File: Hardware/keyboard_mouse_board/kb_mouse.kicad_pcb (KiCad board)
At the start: 2 copper layers, 80.8 x 60.1 mm, 27 parts, among them J1 Conn_01x40, J3 AVR-ISP-6, U1 74HC74, U2 ATmega328P-P, U3 DS1307+, U4 74HC245, Y1 32,768kHz

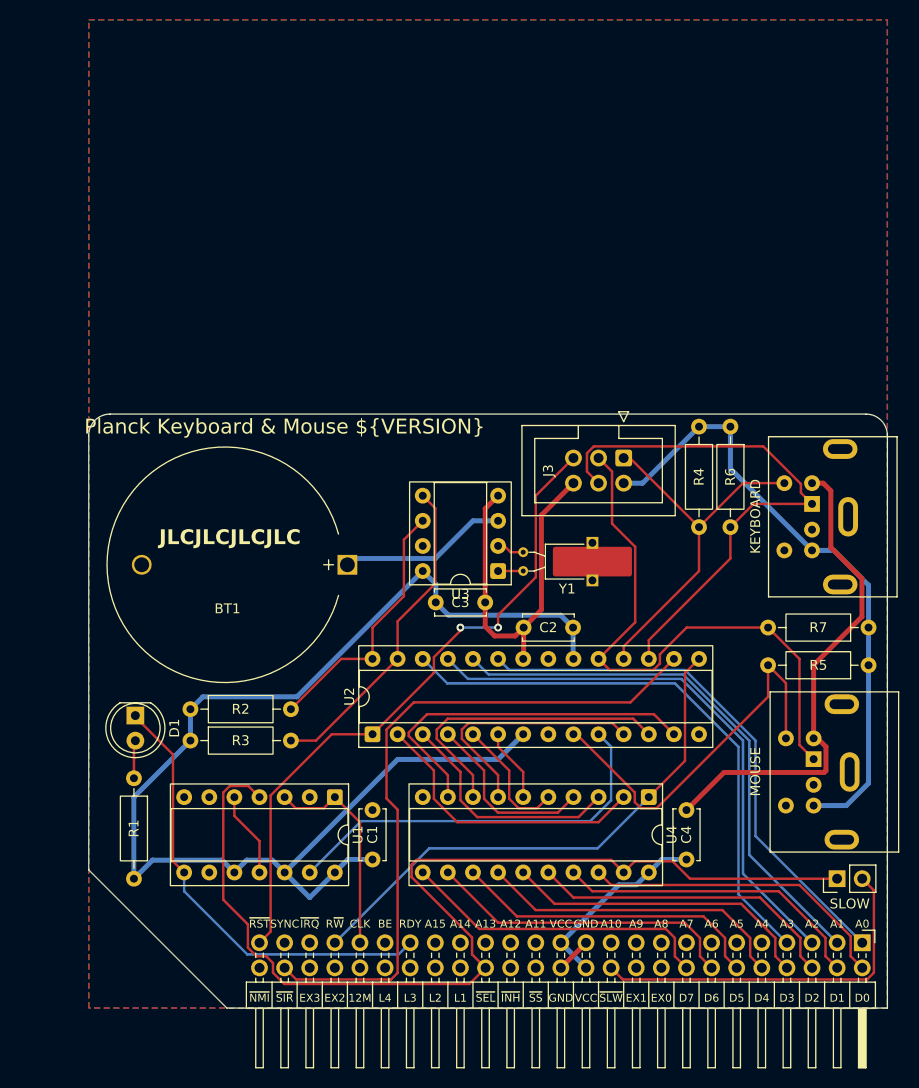
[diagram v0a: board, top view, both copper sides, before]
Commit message: RDY latch fix
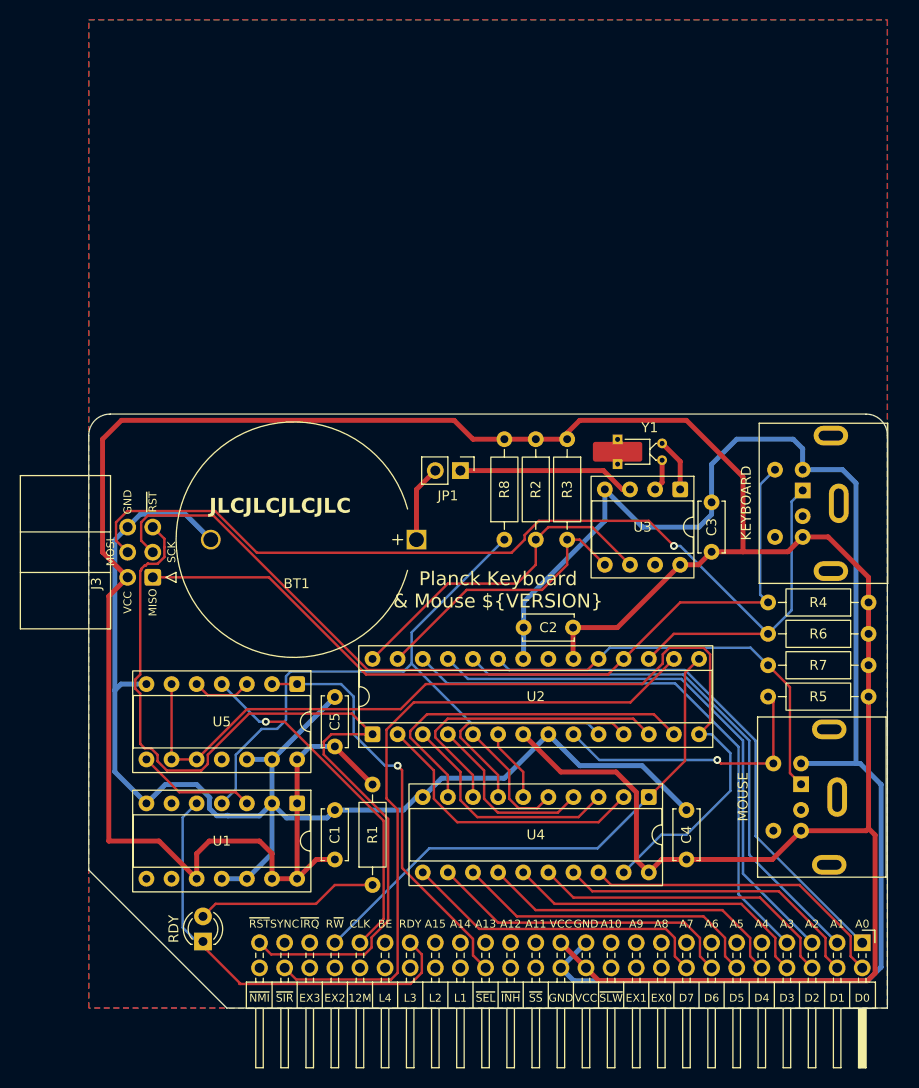
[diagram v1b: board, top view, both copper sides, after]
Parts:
- removed D1: LED, LED_THT:LED_D5.0mm
- removed SLOW: Conn_01x02, Connector_PinHeader_2.54mm:PinHeader_1x02_P2.54mm_Vertical
- added C5: 100n, Capacitor_THT:C_Disc_D5.0mm_W2.5mm_P5.00mm, F.Cu at (130.2, 111.1)
- added JP1: CLK_RESET, Connector_PinHeader_2.54mm:PinHeader_1x02_P2.54mm_Vertical, F.Cu at (142.9, 83.2)
- added R8: 10k, Resistor_THT:R_Axial_DIN0207_L6.3mm_D2.5mm_P10.16mm_Horizontal, F.Cu at (147.3, 90.2)
- added RDY: LED, LED_THT:LED_D3.0mm, F.Cu at (116.8, 130.8)
- added U5: 74HC00, Package_DIP:DIP-14_W7.62mm_Socket, F.Cu at (126.4, 104.8)
- J3: footprint Connector_IDC:IDC-Header_2x03_P2.54mm_Vertical -> Connector_IDC:IDC-Header_2x03_P2.54mm_Horizontal
- Y1: footprint Crystal:Crystal_C38-LF_D3.0mm_L8.0mm_Horizontal_1EP_style2 -> Crystal:Crystal_DS15_D1.5mm_L5.0mm_Horizontal_1EP_style2
- moved J3 49.1 mm to (111.8, 94.0), turned to 180 degrees
- moved R3 48.8 mm to (153.7, 80.0), turned to -90 degrees
- moved R2 44.3 mm to (150.5, 80.0), turned to -90 degrees
- moved C3 28.4 mm to (168.3, 91.4), turned to 90 degrees
- moved R1 26.4 mm to (134.0, 125.1), turned to 90 degrees
- moved R6 25.2 mm to (184.2, 99.7), turned to 180 degrees
- moved R4 24.7 mm to (184.2, 96.5), turned to 180 degrees
- moved U3 20.2 mm to (165.1, 85.1), turned to -90 degrees
- moved Y1 19.1 mm to (163.3, 80.4), turned to -90 degrees
- moved BT1 7.43 mm to (138.4, 90.2)
- moved U1 3.87 mm to (126.4, 116.8)
- moved C1 3.81 mm to (130.2, 122.5)
- moved LOGO 3.81 mm to (125.1, 81.2)
- moved OPENHARDWARE 3.81 mm to (121.6, 92.3)
- moved R7 3.81 mm to (184.2, 102.9)
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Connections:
- U1 pad 1: CLK -> +5V
- U1 pad 11: Net-(U1A-Q) -> GND
- U1 pad 12: +5V -> GND
- U1 pad 13: RDY_STROBE -> +5V
- U1 pad 3: CLK -> CS
- U1 pad 4: ~{SLOT_SEL} -> RDY_STROBE
- U1 pad 5: Net-(U1A-Q) -> RDY
- U1 pad 8: RDY -> unconnected-(U1B-~{Q}-Pad8)
- U2 pad 14: CSEL -> ~{CS}
- U3 pad 3: Net-(BT1-+) -> Net-(JP1-A)
- U4 pad 19: ~{SLOT_SEL} -> ~{CS}
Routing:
- net GND: track 92.2 -> 285.9 mm
- net +5V: track 212.2 -> 332.3 mm
- net ~{CS}: track 0.00 -> 98.1 mm
- net ~{SLOT_SEL}: track 106.4 -> 42.5 mm, vias 0 -> 1
- net KBD DATA: track 55.5 -> 107.1 mm, vias 0 -> 1
- net KBD CLK: track 37.5 -> 83.7 mm
- net ~{SLOW}: track 37.3 -> 0.00 mm
- net MOUSE DATA: track 58.5 -> 88.8 mm
- net ~{RESET}: track 66.8 -> 94.9 mm, vias 2 -> 0
- net RDY_STROBE: track 40.7 -> 68.0 mm
- net Net-(JP1-A): track 0.00 -> 17.9 mm
- net Net-(RDY1-A): track 3.80 -> 18.5 mm
- net CLK: track 21.8 -> 35.4 mm, vias 0 -> 1
- net CS: track 0.00 -> 12.0 mm
- net MOUSE CLK: track 39.4 -> 28.8 mm, vias 0 -> 1
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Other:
- board text added: "MISO"
- board text added: "MOSI"
- board text added: "SCK"
